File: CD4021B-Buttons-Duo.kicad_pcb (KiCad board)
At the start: 2 copper layers, 99.1 x 50.8 mm, 47 parts, among them J1 2.54, J10 JST XH, J11 JST XH, J12 JST XH, J13 JST XH, J14 JST XH, J15 JST XH, J16 JST XH, J17 JST XH, J2 JST XH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

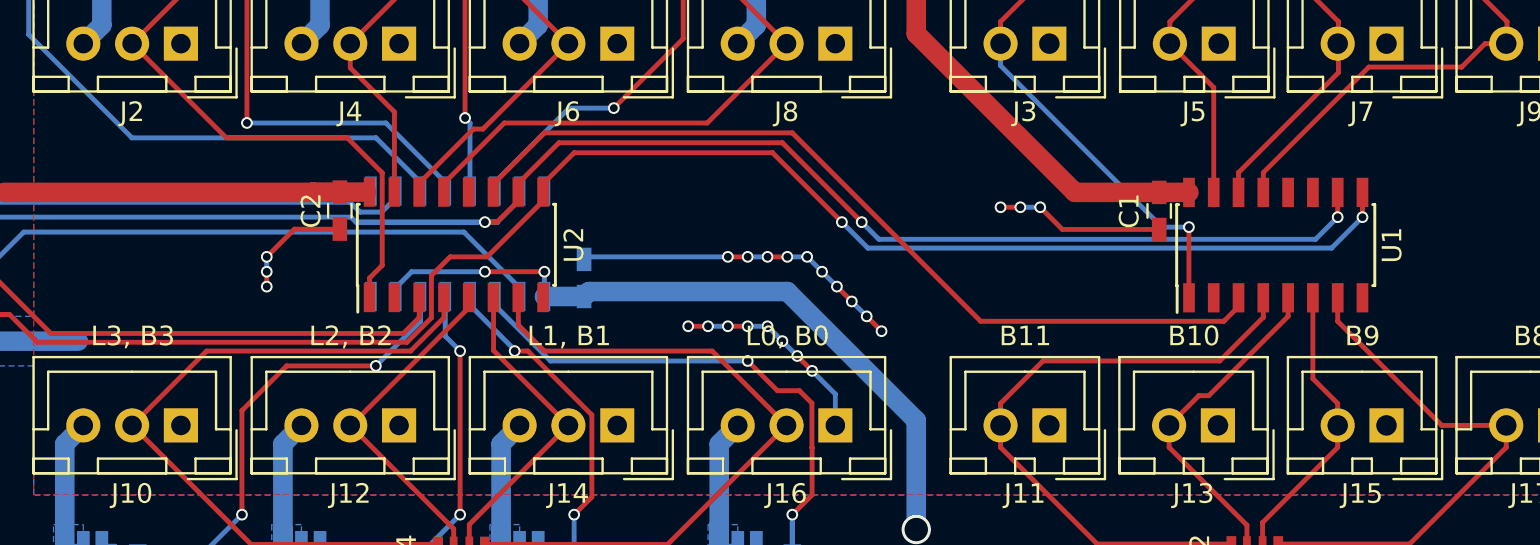
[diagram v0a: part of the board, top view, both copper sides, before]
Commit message: Re-place some via stitches so that they are not under silkscreens
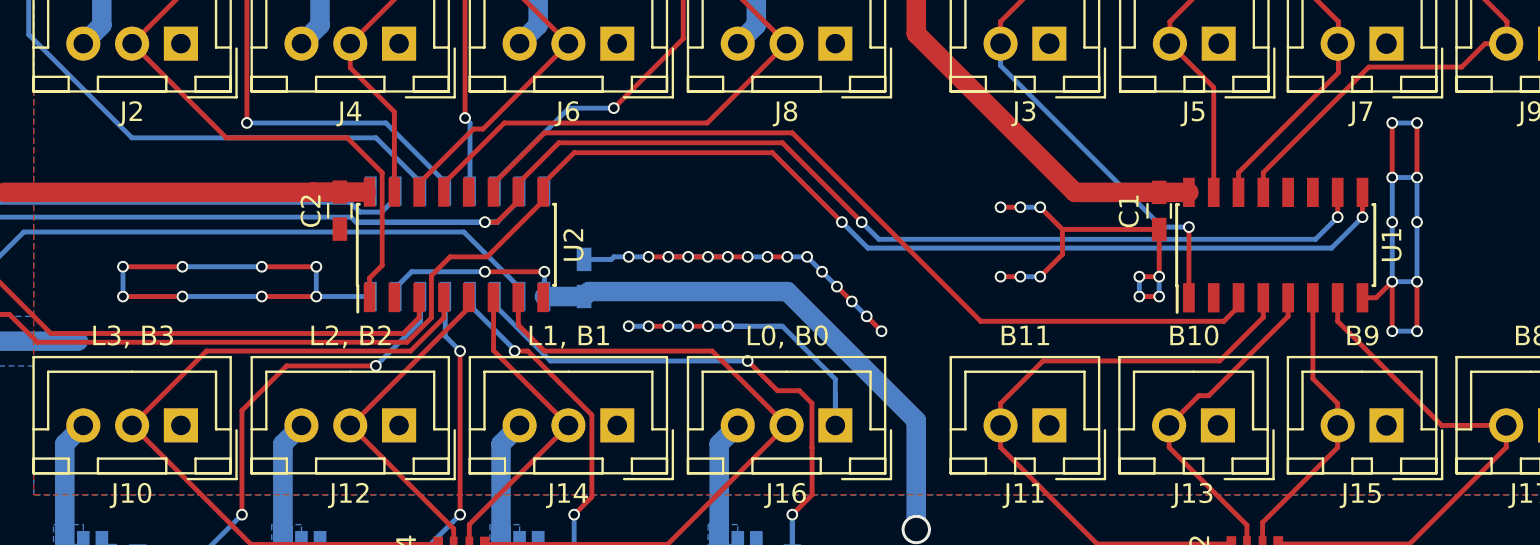
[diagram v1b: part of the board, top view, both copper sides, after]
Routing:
- net GND: track 50.2 -> 119.8 mm, vias 24 -> 49

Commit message: Enable the NC pin as an alternate lamp power pin to (hopefully) allow more current
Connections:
- J1 pad 3: Net-(J1-Pad3) -> /CSI
- J1 pad 4: /CSI -> +12V
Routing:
- net /CSI: track 85.2 -> 82.7 mm
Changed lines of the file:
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@@
 (kicad_pcb (version 4) (host pcbnew 4.0.7)
   (general
-    (links 152)
+    (links 153)
     (no_connects 0)
-    (area 97.409048 78.918999 212.470953 129.869001)
+    (area 105.334999 78.918999 204.545001 129.869001)
     (thickness 1.6)
     (drawings 23)
-    (tracks 452)
+    (tracks 451)
     (zones 0)
     (modules 47)
-    (nets 49)
+    (nets 48)
   )
   (page A4)
   (title_block
     (title "CD4021B Buttons Duo")
-    (date 2018-05-14)
-    (rev 1.1.0)
+    (date 2018-05-16)
+    (rev 1.2.0)
   )
   (layers
@@
   (net 46 "Net-(U2-Pad12)")
   (net 47 "Net-(U3-Pad9)")
-  (net 48 "Net-(J1-Pad3)")
   (net_class Default "This is the default net class."
     (clearance 0.2)
@@
     (add_net /MOSI)
     (add_net /SCK)
-    (add_net "Net-(J1-Pad3)")
     (add_net "Net-(U1-Pad11)")
     (add_net "Net-(U1-Pad12)")
@@
       (net 2 GND))
     (pad 3 thru_hole oval (at 0 2.54 180) (size 1.7 1.7) (drill 1) (layers *.Cu *.Mask)
-      (net 48 "Net-(J1-Pad3)"))
+      (net 6 /CSI))
     (pad 4 thru_hole oval (at 2.54 2.54 180) (size 1.7 1.7) (drill 1) (layers *.Cu *.Mask)
-      (net 6 /CSI))
+      (net 3 +12V))
     (pad 5 thru_hole oval (at 0 5.08 180) (size 1.7 1.7) (drill 1) (layers *.Cu *.Mask)
       (net 5 /MISO))
@@
   (segment (start 135.824454 107.238502) (end 135.824454 108.269546) (width 0.25) (layer F.Cu) (net 5) (status 10))
   (segment (start 116.955978 109.081978) (end 112.268 104.394) (width 0.25) (layer F.Cu) (net 5) (status 20))
-  (segment (start 110.903001 108.109001) (end 109.728 106.934) (width 0.25) (layer F.Cu) (net 6) (status 20))
-  (segment (start 114.838591 108.109001) (end 110.903001 108.109001) (width 0.25) (layer F.Cu) (net 6))
-  (segment (start 135.198422 109.531989) (end 116.261578 109.531989) (width 0.25) (layer F.Cu) (net 6))
-  (segment (start 116.261578 109.531989) (end 114.838591 108.109001) (width 0.25) (layer F.Cu) (net 6))
+  (segment (start 142.174454 101.838502) (end 142.174454 102.288502) (width 0.25) (layer F.Cu) (net 6) (status 30))
+  (segment (start 137.414 105.156) (end 136.449455 106.120545) (width 0.25) (layer F.Cu) (net 6))
+  (segment (start 135.198422 109.531989) (end 116.643989 109.531989) (width 0.25) (layer F.Cu) (net 6))
+  (segment (start 142.174454 102.288502) (end 139.306956 105.156) (width 0.25) (layer F.Cu) (net 6) (status 10))
+  (segment (start 136.449455 106.120545) (end 136.449455 108.280956) (width 0.25) (layer F.Cu) (net 6))
   (segment (start 139.306956 105.156) (end 137.414 105.156) (width 0.25) (layer F.Cu) (net 6))
-  (segment (start 136.449455 106.120545) (end 136.449455 108.280956) (width 0.25) (layer F.Cu) (net 6))
-  (segment (start 137.414 105.156) (end 136.449455 106.120545) (width 0.25) (layer F.Cu) (net 6))
   (segment (start 136.449455 108.280956) (end 135.198422 109.531989) (width 0.25) (layer F.Cu) (net 6))
-  (segment (start 142.174454 101.838502) (end 142.174454 102.288502) (width 0.25) (layer F.Cu) (net 6) (status 30))
-  (segment (start 142.174454 102.288502) (end 139.306956 105.156) (width 0.25) (layer F.Cu) (net 6) (status 10))
+  (segment (start 116.643989 109.531989) (end 114.046 106.934) (width 0.25) (layer F.Cu) (net 6))
+  (segment (start 114.046 106.934) (end 112.268 106.934) (width 0.25) (layer F.Cu) (net 6) (status 20))
   (segment (start 142.174454 101.838502) (end 142.174454 101.411546) (width 0.25) (layer F.Cu) (net 6) (status 30))
   (segment (start 142.174454 101.411546) (end 143.764 99.822) (width 0.25) (layer F.Cu) (net 6) (status 10))
@@
     (polygon
       (pts
-        (xy 196.596 117.348) (xy 116.078 117.348) (xy 116.078 110.744) (xy 109.728 110.744) (xy 109.728 108.204)
-        (xy 116.078 108.204) (xy 116.078 91.694) (xy 196.596 91.694)
+        (xy 196.596 117.348) (xy 116.078 117.348) (xy 116.078 110.744) (xy 113.03 110.744) (xy 113.03 110.236)
+        (xy 109.728 110.236) (xy 109.728 108.712) (xy 113.03 108.712) (xy 113.03 108.204) (xy 116.078 108.204)
+        (xy 116.078 91.694) (xy 196.596 91.694)
       )
     )

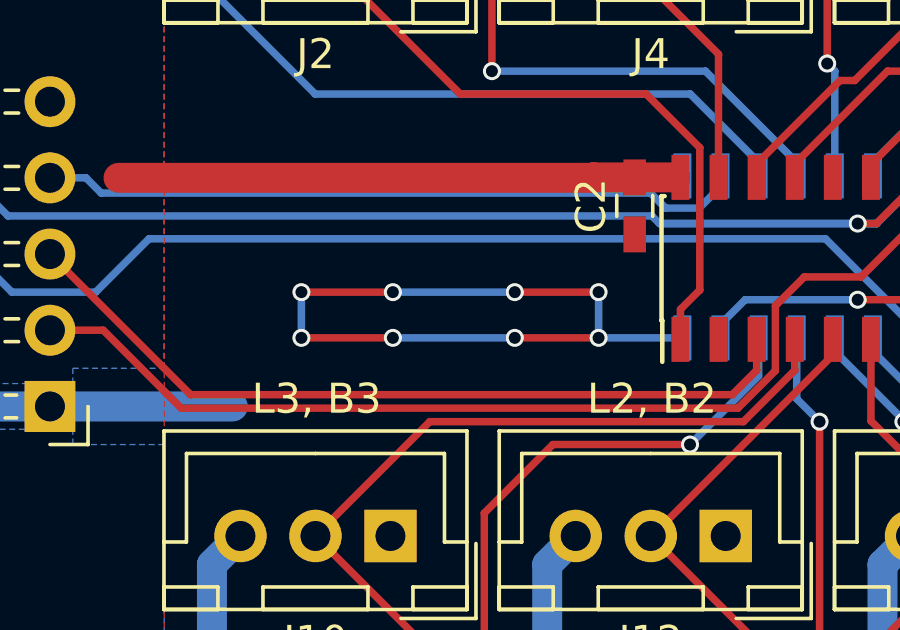
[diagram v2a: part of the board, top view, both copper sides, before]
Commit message: Change the pinout silkscreen
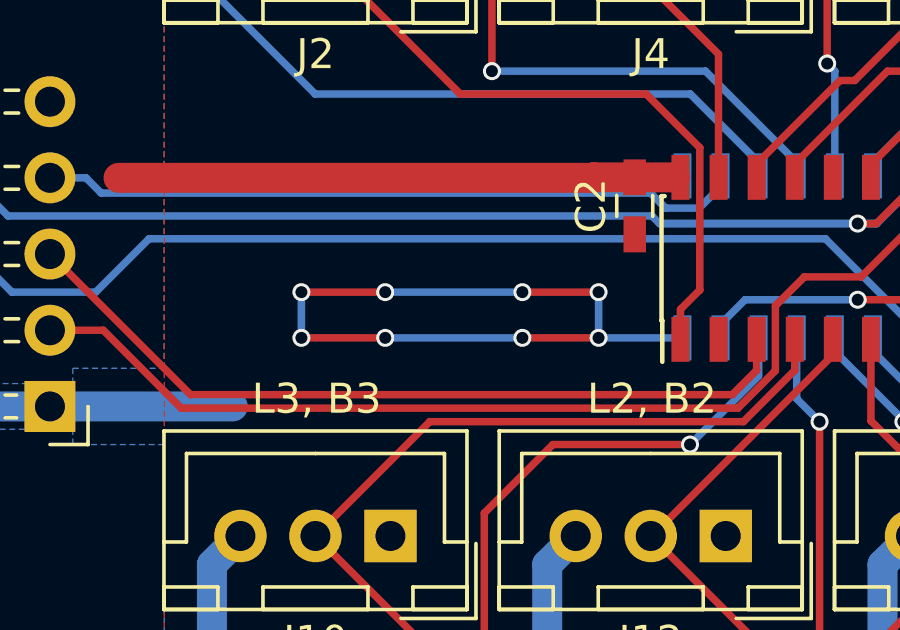
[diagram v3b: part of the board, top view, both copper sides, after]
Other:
- board text added: "VCC CSO MISO CSI GND"
- board text added: "VL SCK MOSI VL GND"
- board text removed: "VCC CSO MISO NC GND"
- board text removed: "VL SCK MOSI CSI GND"
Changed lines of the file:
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@@
     (effects (font (size 1 1) (thickness 0.15)))
   )
-  (gr_text "VCC\nCSO\nMISO\nNC\nGND" (at 127.254 104.394) (layer B.SilkS)
+  (gr_text "VCC\nCSO\nMISO\nCSI\nGND" (at 127.254 104.394) (layer B.SilkS)
     (effects (font (size 1.5 1.5) (thickness 0.3)) (justify left mirror))
   )
-  (gr_text "VL\nSCK  \nMOSI\nCSI\nGND" (at 120.396 104.394) (layer B.SilkS)
+  (gr_text "VL\nSCK  \nMOSI\nVL\nGND" (at 120.396 104.394) (layer B.SilkS)
     (effects (font (size 1.5 1.5) (thickness 0.3)) (justify left mirror))
   )
@@
   (segment (start 131.760454 101.838502) (end 130.385454 101.838502) (width 1) (layer F.Cu) (net 1) (status 10))
   (segment (start 130.385454 101.838502) (end 130.369956 101.854) (width 1) (layer F.Cu) (net 1))
+  (segment (start 123.444 107.188) (end 128.016 107.188) (width 0.25) (layer B.Cu) (net 2))
+  (segment (start 130.556 107.188) (end 128.016 107.188) (width 0.25) (layer F.Cu) (net 2))
+  (via (at 128.016 107.188) (size 0.6) (drill 0.4) (layers F.Cu B.Cu) (net 2))
+  (segment (start 123.444 105.664) (end 128.016 105.664) (width 0.25) (layer B.Cu) (net 2))
+  (segment (start 130.556 105.664) (end 128.016 105.664) (width 0.25) (layer F.Cu) (net 2))
+  (via (at 128.016 105.664) (size 0.6) (drill 0.4) (layers F.Cu B.Cu) (net 2))
+  (segment (start 120.65 105.664) (end 123.444 105.664) (width 0.25) (layer F.Cu) (net 2))
+  (via (at 123.444 105.664) (size 0.6) (drill 0.4) (layers F.Cu B.Cu) (net 2))
+  (segment (start 120.65 107.188) (end 123.444 107.188) (width 0.25) (layer F.Cu) (net 2))
+  (via (at 123.444 107.188) (size 0.6) (drill 0.4) (layers F.Cu B.Cu) (net 2))
   (segment (start 186.944 103.378) (end 186.944 101.092) (width 0.25) (layer B.Cu) (net 2))
   (segment (start 186.944 106.426) (end 186.944 103.378) (width 0.25) (layer B.Cu) (net 2))
@@
   (segment (start 130.556 105.664) (end 130.556 107.188) (width 0.25) (layer B.Cu) (net 2))
   (segment (start 133.35 107.188) (end 130.556 107.188) (width 0.25) (layer B.Cu) (net 2) (status 10))
-  (segment (start 127.761972 107.188) (end 130.556 107.188) (width 0.25) (layer F.Cu) (net 2))
   (via (at 130.556 107.188) (size 0.6) (drill 0.4) (layers F.Cu B.Cu) (net 2))
   (via (at 130.556 105.664) (size 0.6) (drill 0.4) (layers F.Cu B.Cu) (net 2))
-  (segment (start 127.762 105.664) (end 130.556 105.664) (width 0.25) (layer F.Cu) (net 2))
   (segment (start 145.664 105.288) (end 145.796 105.156) (width 0.25) (layer B.Cu) (net 2))
   (segment (start 145.796 105.156) (end 146.557996 105.156) (width 0.25) (layer B.Cu) (net 2))
   (segment (start 144.272 105.288) (end 145.664 105.288) (width 0.25) (layer B.Cu) (net 2) (status 10))
-  (segment (start 120.65 107.188) (end 123.698 107.188) (width 0.25) (layer F.Cu) (net 2))
-  (segment (start 123.698 105.664) (end 127.762 105.664) (width 0.25) (layer B.Cu) (net 2))
-  (via (at 127.762 105.664) (size 0.6) (drill 0.4) (layers F.Cu B.Cu) (net 2))
-  (segment (start 120.65 105.664) (end 123.698 105.664) (width 0.25) (layer F.Cu) (net 2))
-  (via (at 123.698 105.664) (size 0.6) (drill 0.4) (layers F.Cu B.Cu) (net 2))
   (segment (start 120.65 107.188) (end 120.65 105.664) (width 0.25) (layer B.Cu) (net 2))
   (via (at 120.65 105.664) (size 0.6) (drill 0.4) (layers F.Cu B.Cu) (net 2))
-  (segment (start 123.698 107.188) (end 127.761972 107.188) (width 0.25) (layer B.Cu) (net 2))
-  (via (at 127.761972 107.188) (size 0.6) (drill 0.4) (layers F.Cu B.Cu) (net 2))
   (via (at 120.65 107.188) (size 0.6) (drill 0.4) (layers F.Cu B.Cu) (net 2))
-  (via (at 123.698 107.188) (size 0.6) (drill 0.4) (layers F.Cu B.Cu) (net 2))
   (segment (start 151.638 108.712) (end 154.432 108.712) (width 0.25) (layer B.Cu) (net 2))
   (segment (start 154.432 108.712) (end 157.146 111.426) (width 0.25) (layer B.Cu) (net 2))

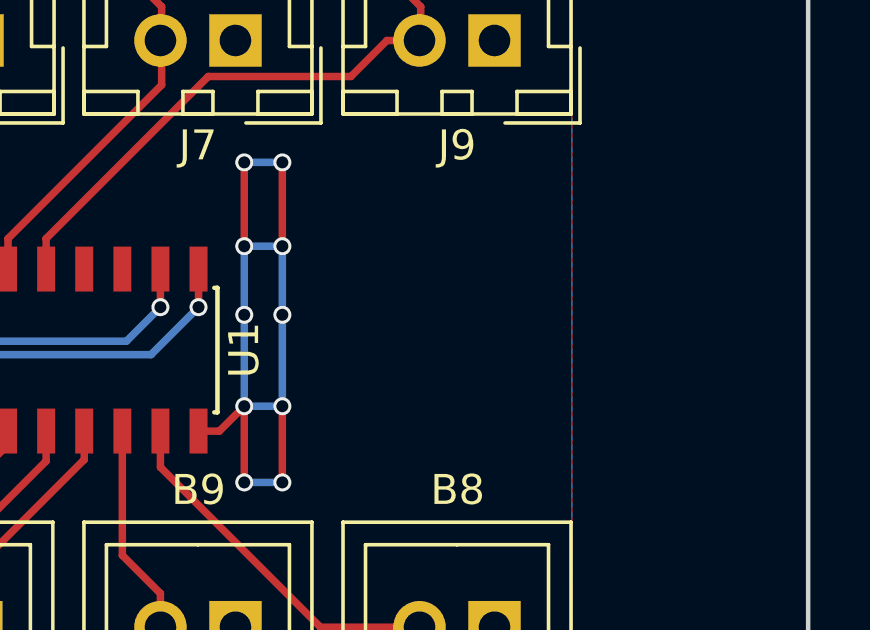
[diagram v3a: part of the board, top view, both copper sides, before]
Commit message: Add open source hardware logo because why not
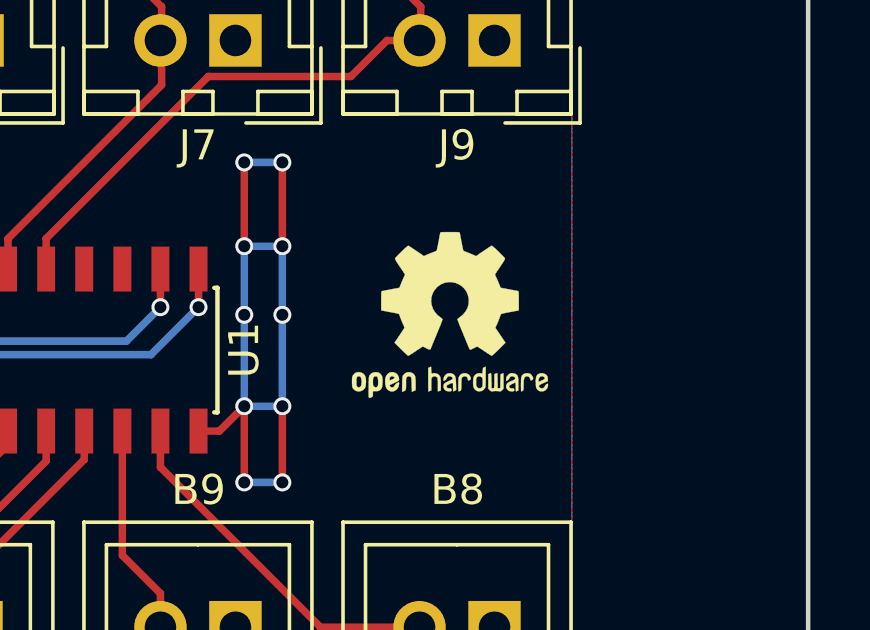
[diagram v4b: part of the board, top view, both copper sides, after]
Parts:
- added REF***: OSHW-Logo2_7.3x6mm_SilkScreen, Symbols:OSHW-Logo2_7.3x6mm_SilkScreen, F.Cu at (192.5, 103.4)

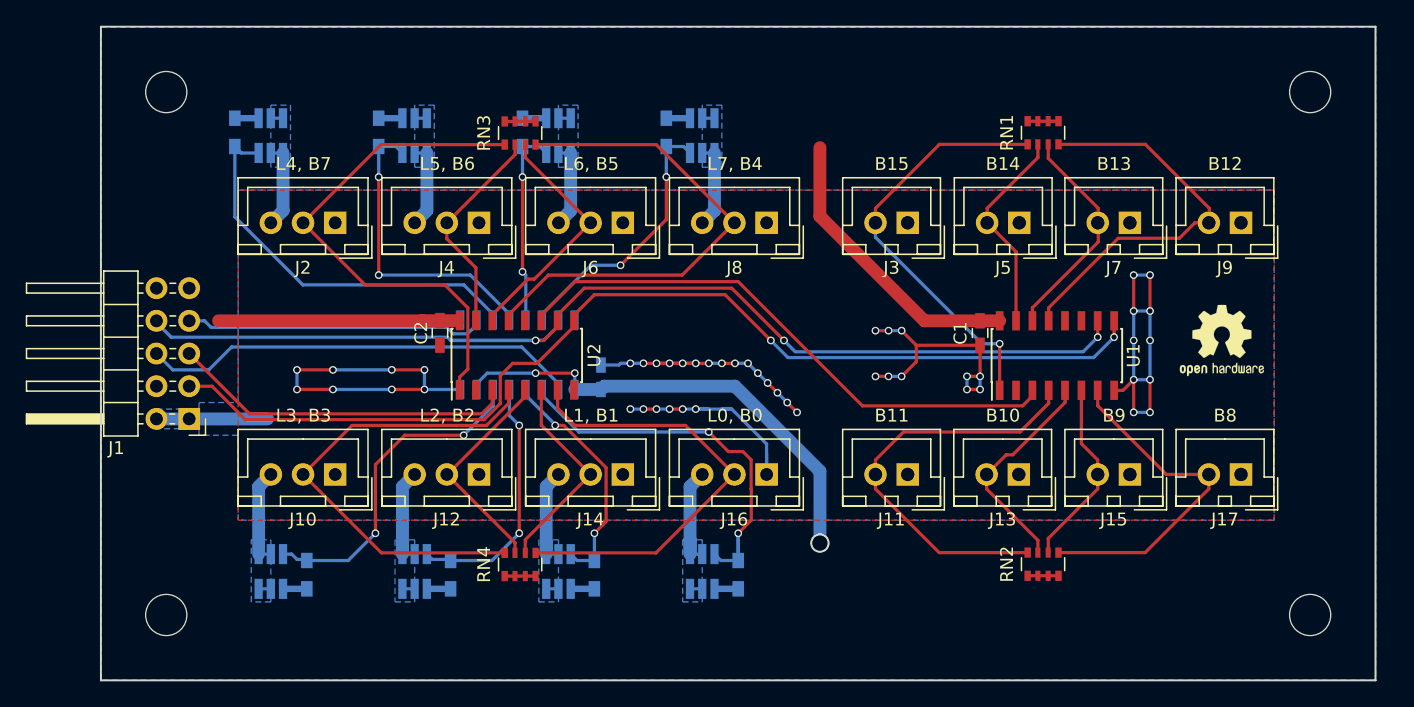
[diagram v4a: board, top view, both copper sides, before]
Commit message: Enlarge grond plane, adjust logo positioning
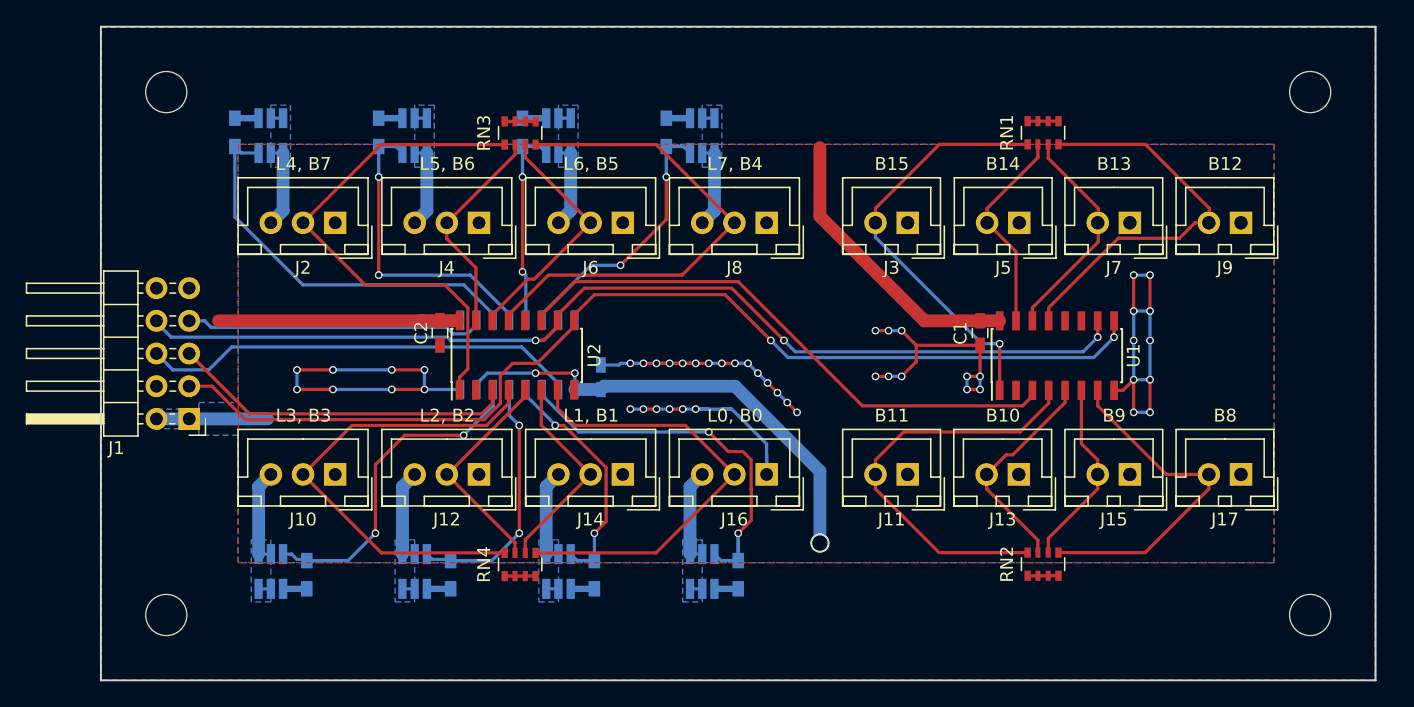
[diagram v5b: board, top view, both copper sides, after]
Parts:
- added REF***: KiCad-Logo2_6mm_SilkScreen, Symbols:KiCad-Logo2_6mm_SilkScreen, B.Cu at (181.6, 125.0)
- REF***: moved to B.Cu
- moved REF*** 31.1 mm to (170.4, 125.2), turned to 180 degrees
